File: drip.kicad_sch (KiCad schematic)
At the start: 79 parts, among them J1 ISP, Q1 2n2907, Q2 2n2907, Q3 2n2907, Q4 2n2907, Q5 2n2907, Q6 2n2907, Q7 2n2907, Q8 2n2907, U1 74LS138, U2 5641AS-4Digit-7Segment, U3 5641AS-4Digit-7Segment, U4 MSP430G2553IN20

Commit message: Fix inverted select
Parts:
- R1, R2, R3, R4, R5, R6, R7, R8: value R_Small_US -> 10kΩ
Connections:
- net ~{SEL_0} renamed SEL_0
- net ~{SEL_1} renamed SEL_1
- net ~{SEL_2} renamed SEL_2
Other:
- note removed: "Software will have to take care of inverting these ~{selects}, not sure why the '251 is active-high selects but active-low ~{OE}"
- moved on the sheet: SW?

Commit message: Use 10k on 7seg data lines
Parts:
- R? (x8): value R_Small_US -> 10kΩ
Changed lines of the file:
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@@
     (in_bom yes) (on_board yes)
     (property "Reference" "R?" (id 0) (at 389.89 350.52 90))
-    (property "Value" "R_Small_US" (id 1) (at 393.065 347.98 90)
+    (property "Value" "10kΩ" (id 1) (at 393.065 347.98 90)
       (effects (font (size 1.27 1.27)) hide)
     )
@@
     (in_bom yes) (on_board yes)
     (property "Reference" "R?" (id 0) (at 389.89 353.06 90))
-    (property "Value" "R_Small_US" (id 1) (at 393.065 350.52 90)
+    (property "Value" "10kΩ" (id 1) (at 393.065 350.52 90)
       (effects (font (size 1.27 1.27)) hide)
     )
@@
     (in_bom yes) (on_board yes)
     (property "Reference" "R?" (id 0) (at 389.89 337.82 90))
-    (property "Value" "R_Small_US" (id 1) (at 393.065 335.28 90)
+    (property "Value" "10kΩ" (id 1) (at 393.065 335.28 90)
       (effects (font (size 1.27 1.27)) hide)
     )
@@
     (in_bom yes) (on_board yes)
     (property "Reference" "R?" (id 0) (at 389.89 345.44 90))
-    (property "Value" "R_Small_US" (id 1) (at 393.065 342.9 90)
+    (property "Value" "10kΩ" (id 1) (at 393.065 342.9 90)
       (effects (font (size 1.27 1.27)) hide)
     )
@@
     (in_bom yes) (on_board yes)
     (property "Reference" "R?" (id 0) (at 389.89 340.36 90))
-    (property "Value" "R_Small_US" (id 1) (at 393.065 337.82 90)
+    (property "Value" "10kΩ" (id 1) (at 393.065 337.82 90)
       (effects (font (size 1.27 1.27)) hide)
     )
@@
     (in_bom yes) (on_board yes)
     (property "Reference" "R?" (id 0) (at 389.89 342.9 90))
-    (property "Value" "R_Small_US" (id 1) (at 393.065 340.36 90)
+    (property "Value" "10kΩ" (id 1) (at 393.065 340.36 90)
       (effects (font (size 1.27 1.27)) hide)
     )
@@
     (in_bom yes) (on_board yes)
     (property "Reference" "R?" (id 0) (at 389.89 355.6 90))
-    (property "Value" "R_Small_US" (id 1) (at 393.065 353.06 90)
+    (property "Value" "10kΩ" (id 1) (at 393.065 353.06 90)
       (effects (font (size 1.27 1.27)) hide)
     )
@@
     (in_bom yes) (on_board yes)
     (property "Reference" "R?" (id 0) (at 389.89 347.98 90))
-    (property "Value" "R_Small_US" (id 1) (at 393.065 345.44 90)
+    (property "Value" "10kΩ" (id 1) (at 393.065 345.44 90)
       (effects (font (size 1.27 1.27)) hide)
     )
@@
     )
     (path "/128bf98d-4eb5-4284-a328-b2f2b3a6268d"
-      (reference "R?") (unit 1) (value "R_Small_US") (footprint "")
+      (reference "R?") (unit 1) (value "10kΩ") (footprint "")
     )
     (path "/133256af-5e9c-4ec4-8f48-0c62a62f35a2"
@@
     )
     (path "/2f5897f7-1c6d-446b-b01c-4031ddc7b6be"
-      (reference "R?") (unit 1) (value "R_Small_US") (footprint "")
+      (reference "R?") (unit 1) (value "10kΩ") (footprint "")
     )
     (path "/84a2d95c-13c3-4b21-898b-311e7d2d95d6"
@@
     )
     (path "/aeb5d3f2-9ac3-4a75-b1f7-273f9a74747c"
-      (reference "R?") (unit 1) (value "R_Small_US") (footprint "")
+      (reference "R?") (unit 1) (value "10kΩ") (footprint "")
     )
     (path "/cc6b9ca2-f2be-411a-abca-616da95a9573"
-      (reference "R?") (unit 1) (value "R_Small_US") (footprint "")
+      (reference "R?") (unit 1) (value "10kΩ") (footprint "")
     )
     (path "/d165f18e-ff01-4b84-97a3-752bec5ec522"
-      (reference "R?") (unit 1) (value "R_Small_US") (footprint "")
+      (reference "R?") (unit 1) (value "10kΩ") (footprint "")
     )
     (path "/d589e088-d37a-4dcc-ac92-1003de4ca876"
-      (reference "R?") (unit 1) (value "R_Small_US") (footprint "")
+      (reference "R?") (unit 1) (value "10kΩ") (footprint "")
     )
     (path "/ecb6ca29-bc81-4d86-a7b8-609658eb9999"
-      (reference "R?") (unit 1) (value "R_Small_US") (footprint "")
+      (reference "R?") (unit 1) (value "10kΩ") (footprint "")
     )
     (path "/fbf2789b-7963-4d3a-abcb-00186b4a53d7"
-      (reference "R?") (unit 1) (value "R_Small_US") (footprint "")
+      (reference "R?") (unit 1) (value "10kΩ") (footprint "")
     )
     (path "/09aec712-8ac2-485c-b85f-1d503ee77605"

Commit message: Button footprint, maybe
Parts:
- R1, R2, R3, R4, R5, R6, R7, R8: footprint (none) -> Resistor_THT:R_Axial_DIN0207_L6.3mm_D2.5mm_P10.16mm_Horizontal
- R10, R11, R12, R13, R14, R15, R16, R17, R18, R19, R9: renamed from R?; footprint (none) -> Resistor_THT:R_Axial_DIN0207_L6.3mm_D2.5mm_P10.16mm_Horizontal
- SW1, SW10, SW11, SW12, SW13, SW14, SW15, SW16, SW17, SW18, SW19, SW2, SW20, SW21, SW22, SW23, SW24, SW25, SW26, SW27, SW28, SW29, SW3, SW30, SW31, SW32, SW33, SW34, SW35, SW36, SW37, SW4, SW5, SW6, SW7, SW8, SW9: renamed from SW?; footprint (none) -> DripButtons:8mm_G77_Push
- U1: value 74LS138 -> 74HC138
- U5: renamed from U?; value 74LS251 -> 74HC251
- U6: renamed from U?; value 74LS138 -> 74HC138
- U7: renamed from U?; value 74LS595 -> 74HC595
- gave numbers to parts that had none: 3
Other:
- note removed: "TODO: Can I run a 74ls138 on 3.3v?"

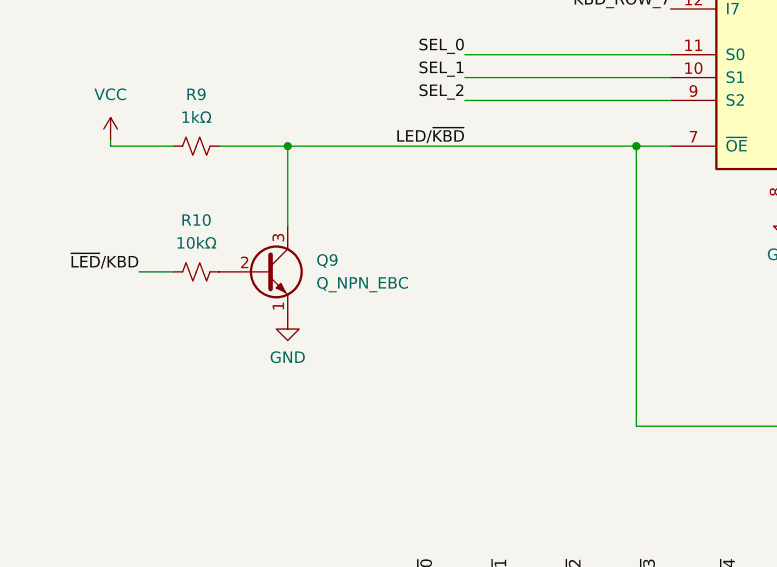
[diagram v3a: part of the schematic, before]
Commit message: Fully footprinted schematic
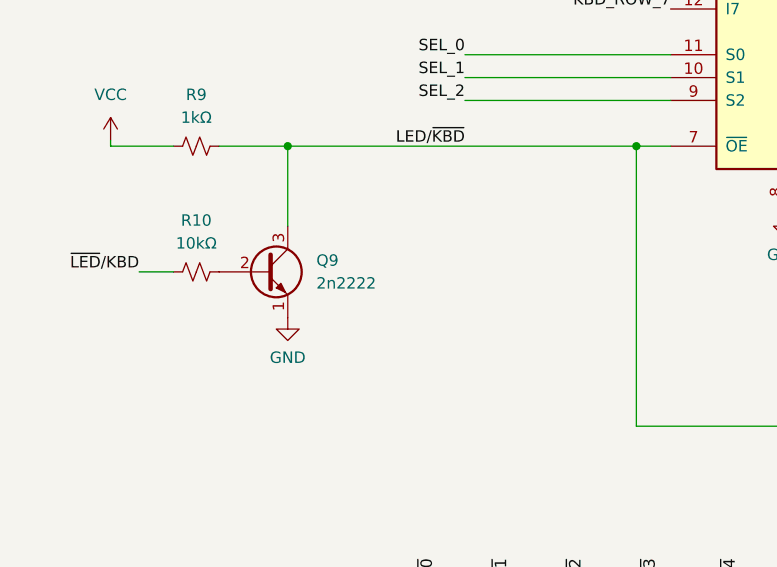
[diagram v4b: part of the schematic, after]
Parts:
- JP5, JP6: footprint (none) -> Jumper:SolderJumper-2_P1.3mm_Bridged2Bar_RoundedPad1.0x1.5mm
- Q9: value Q_NPN_EBC -> 2n2222; footprint (none) -> Package_TO_SOT_THT:TO-92L_Inline
- U5, U6: footprint (none) -> Package_DIP:DIP-16_W7.62mm_Socket_LongPads
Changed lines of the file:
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@@
       (effects (font (size 1.27 1.27)) hide)
     )
-    (property "Footprint" "" (id 2) (at 347.345 354.33 0)
+    (property "Footprint" "Jumper:SolderJumper-2_P1.3mm_Bridged2Bar_RoundedPad1.0x1.5mm" (id 2) (at 347.345 354.33 0)
       (effects (font (size 1.27 1.27)) hide)
     )
@@
       (effects (font (size 1.27 1.27)) (justify left))
     )
-    (property "Footprint" "" (id 2) (at 147.32 236.22 0)
+    (property "Footprint" "Package_DIP:DIP-16_W7.62mm_Socket_LongPads" (id 2) (at 147.32 236.22 0)
       (effects (font (size 1.27 1.27)) hide)
     )
@@
       (effects (font (size 1.27 1.27)) (justify left))
     )
-    (property "Footprint" "" (id 2) (at 111.76 197.485 0)
+    (property "Footprint" "Package_DIP:DIP-16_W7.62mm_Socket_LongPads" (id 2) (at 111.76 197.485 0)
       (effects (font (size 1.27 1.27)) hide)
     )
@@
       (effects (font (size 1.27 1.27)) hide)
     )
-    (property "Footprint" "" (id 2) (at 335.28 351.79 0)
+    (property "Footprint" "Jumper:SolderJumper-2_P1.3mm_Bridged2Bar_RoundedPad1.0x1.5mm" (id 2) (at 335.28 351.79 0)
       (effects (font (size 1.27 1.27)) hide)
     )
@@
       (effects (font (size 1.27 1.27)) (justify left))
     )
-    (property "Value" "Q_NPN_EBC" (id 1) (at 59.69 230.5049 0)
-      (effects (font (size 1.27 1.27)) (justify left))
-    )
-    (property "Footprint" "" (id 2) (at 59.055 226.695 0)
+    (property "Value" "2n2222" (id 1) (at 59.69 230.5049 0)
+      (effects (font (size 1.27 1.27)) (justify left))
+    )
+    (property "Footprint" "Package_TO_SOT_THT:TO-92L_Inline" (id 2) (at 59.055 226.695 0)
       (effects (font (size 1.27 1.27)) hide)
     )
@@
     )
     (path "/61044d30-1770-4c3d-b97d-7db5b532ad09"
-      (reference "JP5") (unit 1) (value "Jumper_2_Bridged") (footprint "")
+      (reference "JP5") (unit 1) (value "Jumper_2_Bridged") (footprint "Jumper:SolderJumper-2_P1.3mm_Bridged2Bar_RoundedPad1.0x1.5mm")
     )
     (path "/0445bf15-da07-48c0-a8de-26862fcf9018"
-      (reference "JP6") (unit 1) (value "Jumper_2_Bridged") (footprint "")
+      (reference "JP6") (unit 1) (value "Jumper_2_Bridged") (footprint "Jumper:SolderJumper-2_P1.3mm_Bridged2Bar_RoundedPad1.0x1.5mm")
     )
     (path "/1d72346c-b99b-4c6d-9e88-bc877176be56"
@@
     )
     (path "/939ab6aa-dbe9-43c6-965a-086e911795f2"
-      (reference "Q9") (unit 1) (value "Q_NPN_EBC") (footprint "")
+      (reference "Q9") (unit 1) (value "2n2222") (footprint "Package_TO_SOT_THT:TO-92L_Inline")
     )
     (path "/145b74ec-bedb-46ee-9f86-14f013c61016"
@@
     )
     (path "/164ec3c1-bd7a-4bb1-8613-debffd171eb8"
-      (reference "U5") (unit 1) (value "74HC251") (footprint "")
+      (reference "U5") (unit 1) (value "74HC251") (footprint "Package_DIP:DIP-16_W7.62mm_Socket_LongPads")
     )
     (path "/117cc87e-99c8-46c5-b889-87194d87a2f8"
-      (reference "U6") (unit 1) (value "74HC138") (footprint "")
+      (reference "U6") (unit 1) (value "74HC138") (footprint "Package_DIP:DIP-16_W7.62mm_Socket_LongPads")
     )
     (path "/9996183c-20da-4f1d-bad6-9ad27b56213d"

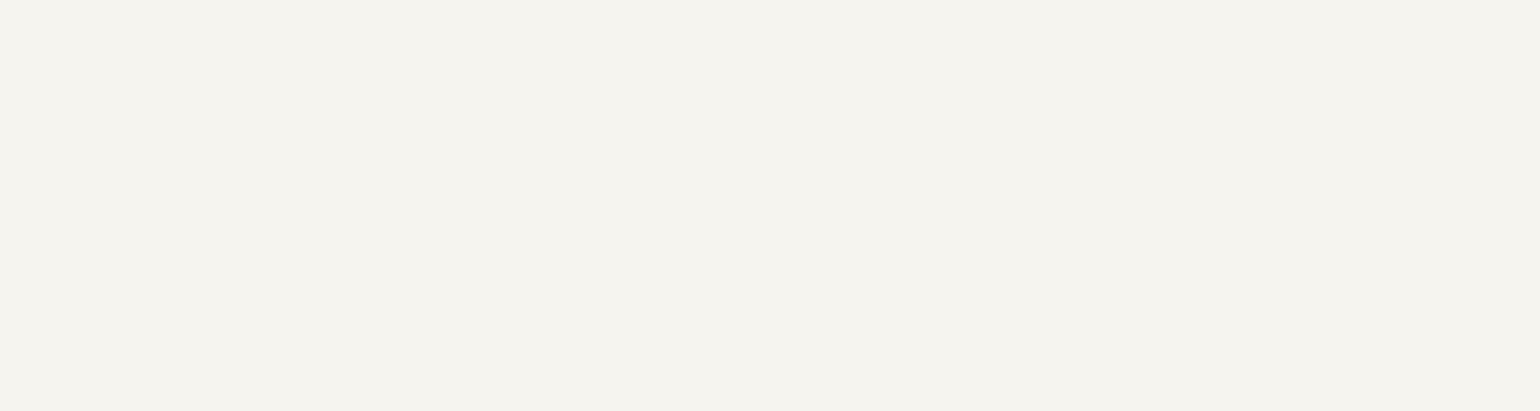
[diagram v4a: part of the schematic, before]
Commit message: 2xAA holder
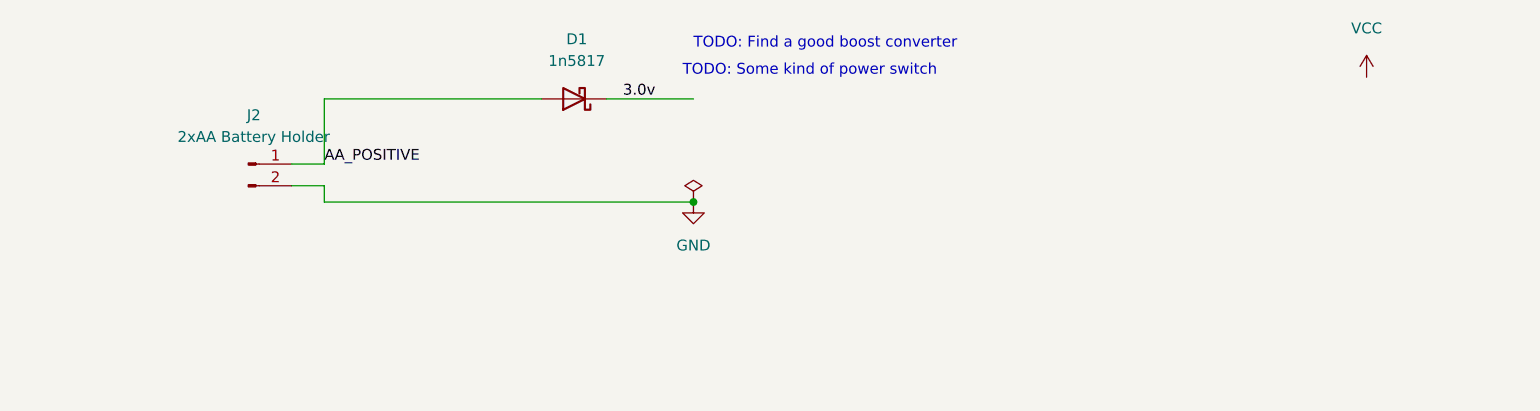
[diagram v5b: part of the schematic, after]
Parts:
- added D1: 1n5817, Diode_THT:D_DO-41_SOD81_P10.16mm_Horizontal, symbol Device:D_Schottky
- added J2: 2xAA Battery Holder, Battery:BatteryHolder_MPD_BC2AAPC_2xAA, symbol Connector:Conn_01x02_Male
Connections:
- net GND: now also J2.2 (Pin_2)
- new net 3.0v: D1.1 (K)
- new net AA_POSITIVE: D1.2 (A), J2.1 (Pin_1)
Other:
- note added: "TODO: Find a good boost converter"
- note added: "TODO: Some kind of power switch"
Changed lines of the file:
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@@
   (junction (at 73.025 351.155) (diameter 0) (color 0 0 0 0)
+  )
+  (junction (at 107.95 74.295) (diameter 0) (color 0 0 0 0)
   )
   (junction (at 454.66 201.93) (diameter 0) (color 0 0 0 0)
@@
     (stroke (width 0) (type default) (color 0 0 0 0))
   )
+  (wire (pts (xy 90.17 62.23) (xy 64.77 62.23))
+    (stroke (width 0) (type default) (color 0 0 0 0))
+  )
   (wire (pts (xy 408.94 349.25) (xy 459.74 349.25))
     (stroke (width 0) (type default) (color 0 0 0 0))
@@
     (stroke (width 0) (type default) (color 0 0 0 0))
   )
+  (wire (pts (xy 60.96 69.85) (xy 64.77 69.85))
+    (stroke (width 0) (type default) (color 0 0 0 0))
+  )
   (wire (pts (xy 106.68 325.755) (xy 106.68 338.455))
     (stroke (width 0) (type default) (color 0 0 0 0))
@@
     (stroke (width 0) (type default) (color 0 0 0 0))
   )
+  (wire (pts (xy 64.77 62.23) (xy 64.77 69.85))
+    (stroke (width 0) (type default) (color 0 0 0 0))
+  )
   (wire (pts (xy 398.78 296.545) (xy 398.78 306.07))
     (stroke (width 0) (type default) (color 0 0 0 0))
@@
     (stroke (width 0) (type default) (color 0 0 0 0))
   )
+  (wire (pts (xy 64.77 74.295) (xy 107.95 74.295))
+    (stroke (width 0) (type default) (color 0 0 0 0))
+  )
   (wire (pts (xy 379.73 341.63) (xy 390.525 341.63))
     (stroke (width 0) (type default) (color 0 0 0 0))
@@
     (stroke (width 0) (type default) (color 0 0 0 0))
   )
+  (wire (pts (xy 97.79 62.23) (xy 107.95 62.23))
+    (stroke (width 0) (type default) (color 0 0 0 0))
+  )
+  (wire (pts (xy 64.77 72.39) (xy 64.77 74.295))
+    (stroke (width 0) (type default) (color 0 0 0 0))
+  )
   (wire (pts (xy 346.71 339.09) (xy 359.41 339.09))
     (stroke (width 0) (type default) (color 0 0 0 0))
@@
     (stroke (width 0) (type default) (color 0 0 0 0))
   )
+  (wire (pts (xy 60.96 72.39) (xy 64.77 72.39))
+    (stroke (width 0) (type default) (color 0 0 0 0))
+  )
   (wire (pts (xy 167.005 127.635) (xy 161.29 127.635))
     (stroke (width 0) (type default) (color 0 0 0 0))
@@
     (stroke (width 0) (type default) (color 0 0 0 0))
   )
+  (text "TODO: Some kind of power switch" (at 106.68 59.69 0)
+    (effects (font (size 1.27 1.27)) (justify left bottom))
+  )
   (text "TODO: Does 0..7 make more sense than 7..0?" (at 324.485 279.4 0)
+    (effects (font (size 1.27 1.27)) (justify left bottom))
+  )
+  (text "TODO: Find a good boost converter" (at 107.95 56.515 0)
     (effects (font (size 1.27 1.27)) (justify left bottom))
   )
@@
     (effects (font (size 1.27 1.27)) (justify right bottom))
   )
+  (label "AA_POSITIVE" (at 64.77 69.85 0)
+    (effects (font (size 1.27 1.27)) (justify left bottom))
+  )
   (label "SEL_0" (at 337.82 266.7 180)
     (effects (font (size 1.27 1.27)) (justify right bottom))
@@
   (label "~{RST}" (at 146.685 178.435 180)
     (effects (font (size 1.27 1.27)) (justify right bottom))
+  )
+  (label "3.0v" (at 99.695 62.23 0)
+    (effects (font (size 1.27 1.27)) (justify left bottom))
   )
   (symbol (lib_id "power:VCC") (at 147.32 220.98 0) (unit 1)
@@
     (pin "2")
   )
+  (symbol (lib_id "Connector:Conn_01x02_Male") (at 55.88 69.85 0) (unit 1)
+    (in_bom yes) (on_board yes) (fields_autoplaced)
+    (property "Reference" "J2" (id 0) (at 56.515 64.135 0))
+    (property "Value" "2xAA Battery Holder" (id 1) (at 56.515 66.675 0))
+    (property "Footprint" "Battery:BatteryHolder_MPD_BC2AAPC_2xAA" (id 2) (at 55.88 69.85 0)
+      (effects (font (size 1.27 1.27)) hide)
+    )
+    (property "Datasheet" "~" (id 3) (at 55.88 69.85 0)
+      (effects (font (size 1.27 1.27)) hide)
+    )
+    (property "DigiKey" "BC2AAPC-ND " (id 4) (at 55.88 69.85 0)
+      (effects (font (size 1.27 1.27)) hide)
+    )
+    (pin "1")
+    (pin "2")
+  )
   (symbol (lib_id "5641AS:5641AS-4Digit-7Segment") (at 392.43 316.23 90) (unit 1)
     (in_bom yes) (on_board yes) (fields_autoplaced)
@@
     (pin "1")
   )
+  (symbol (lib_id "power:GND") (at 107.95 74.295 0) (unit 1)
+    (in_bom yes) (on_board yes) (fields_autoplaced)
+    (property "Reference" "#PWR0119" (id 0) (at 107.95 80.645 0)
+      (effects (font (size 1.27 1.27)) hide)
+    )
+    (property "Value" "GND" (id 1) (at 107.95 79.375 0))
+    (property "Footprint" "" (id 2) (at 107.95 74.295 0)
+      (effects (font (size 1.27 1.27)) hide)
+    )
+    (property "Datasheet" "" (id 3) (at 107.95 74.295 0)
+      (effects (font (size 1.27 1.27)) hide)
+    )
+    (pin "1")
+  )
   (symbol (lib_id "Switch:SW_Push_45deg") (at 78.74 323.215 0) (unit 1)
     (in_bom yes) (on_board yes) (fields_autoplaced)
@@
     (pin "1")
   )
+  (symbol (lib_id "power:PWR_FLAG") (at 107.95 74.295 0) (unit 1)
+    (in_bom yes) (on_board yes) (fields_autoplaced)
+    (property "Reference" "#FLG0101" (id 0) (at 107.95 72.39 0)
+      (effects (font (size 1.27 1.27)) hide)
+    )
+    (property "Value" "PWR_FLAG" (id 1) (at 107.95 69.215 0)
+      (effects (font (size 1.27 1.27)) hide)
+    )
+    (property "Footprint" "" (id 2) (at 107.95 74.295 0)
+      (effects (font (size 1.27 1.27)) hide)
+    )
+    (property "Datasheet" "~" (id 3) (at 107.95 74.295 0)
+      (effects (font (size 1.27 1.27)) hide)
+    )
+    (pin "1")
+  )
   (symbol (lib_id "Device:R_Small_US") (at 393.065 339.09 90) (unit 1)
     (in_bom yes) (on_board yes)
@@
     (pin "1")
   )
+  (symbol (lib_id "Device:D_Schottky") (at 93.98 62.23 180) (unit 1)
+    (in_bom yes) (on_board yes) (fields_autoplaced)
+    (property "Reference" "D1" (id 0) (at 94.2975 55.245 0))
+    (property "Value" "1n5817" (id 1) (at 94.2975 57.785 0))
+    (property "Footprint" "Diode_THT:D_DO-41_SOD81_P10.16mm_Horizontal" (id 2) (at 93.98 62.23 0)
+      (effects (font (size 1.27 1.27)) hide)
+    )
+    (property "Datasheet" "~" (id 3) (at 93.98 62.23 0)
+      (effects (font (size 1.27 1.27)) hide)
+    )
+    (pin "1")
+    (pin "2")
+  )
   (symbol (lib_id "Switch:SW_Push_45deg") (at 104.14 335.915 0) (unit 1)
     (in_bom yes) (on_board yes)
@@
     (pin "2")
   )
+  (symbol (lib_id "power:VCC") (at 186.69 59.69 0) (unit 1)
+    (in_bom yes) (on_board yes) (fields_autoplaced)
+    (property "Reference" "#PWR0120" (id 0) (at 186.69 63.5 0)
+      (effects (font (size 1.27 1.27)) hide)
+    )
+    (property "Value" "VCC" (id 1) (at 186.69 53.975 0))
+    (property "Footprint" "" (id 2) (at 186.69 59.69 0)
+      (effects (font (size 1.27 1.27)) hide)
+    )
+    (property "Datasheet" "" (id 3) (at 186.69 59.69 0)
+      (effects (font (size 1.27 1.27)) hide)
+    )
+    (pin "1")
+  )
   (symbol (lib_id "power:VCC") (at 134.62 167.64 0) (unit 1)
     (in_bom yes) (on_board yes) (fields_autoplaced)
@@
   )
   (symbol_instances
+    (path "/ae489e03-1cd2-4ac6-83a8-f8dbb8a9ca51"
+      (reference "#FLG0101") (unit 1) (value "PWR_FLAG") (footprint "")
+    )
     (path "/a9c0a7a1-1088-4ac8-97de-66e1a8d55f21"
       (reference "#PWR01") (unit 1) (value "VCC") (footprint "")
@@
       (reference "#PWR0118") (unit 1) (value "GND") (footprint "")
     )
+    (path "/7a5f39bb-3cc0-4d87-96dd-8fef6d535b1c"
+      (reference "#PWR0119") (unit 1) (value "GND") (footprint "")
+    )
+    (path "/fe5428c7-929a-4796-bc88-9f54793e3a71"
+      (reference "#PWR0120") (unit 1) (value "VCC") (footprint "")
+    )
+    (path "/e5a84063-5c25-4083-84d8-2c4897914137"
+      (reference "D1") (unit 1) (value "1n5817") (footprint "Diode_THT:D_DO-41_SOD81_P10.16mm_Horizontal")
+    )
     (path "/1316d982-f638-40c6-90fd-9cab7a83850f"
       (reference "J1") (unit 1) (value "ISP") (footprint "Connector_PinHeader_2.54mm:PinHeader_1x04_P2.54mm_Vertical")
     )
+    (path "/6551a886-cb34-4d3d-87fb-4837053adaa5"
+      (reference "J2") (unit 1) (value "2xAA Battery Holder") (footprint "Battery:BatteryHolder_MPD_BC2AAPC_2xAA")
+    )
     (path "/8b7a5ff1-bfc4-473f-a51a-f734693c1551"
